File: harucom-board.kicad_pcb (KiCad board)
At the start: 4 copper layers, 91 x 55 mm, 129 parts, among them J1 GT-USB-7010ASV, J2 10.0QCHTZ6.8, J3 HDA65-N1S1-4000-A, J4 PJ-320D, J5 Grove, J6 Grove, J7 PinSocket_1x06, J8 Conn_01x06, Q1 AO3401A, Q2 2N7002, Q3 AO3401A, SW1 PCM12, SW10 TS-1187, SW11 TS-1187, SW2 TS-1088, SW3 TS-1088, SW4 TS-1187, SW5 TS-1187, SW6 TS-1187, SW7 TS-1187, SW8 TS-1187, SW9 TS-1187, U1 H5VU25UC, U10 H5VU25UC, U11 H5VU25UC, U2 AMS1117-3.3, U3 W25Q128JVS, U4 APS6404L-3SQR-SN, U5 RP2350_60QFN, U6 H5VU25UC, U7 NC7WZ16P6X, U8 H5VU25UC, U9 H5VU25UC, Y1 ABM8-272-T3

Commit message: Rev.2 (260322)
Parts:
- removed C33: 100n, Capacitor_SMD:C_0603_1608Metric
- removed the D7 at (136.8, 124.1)
- removed the D8 at (150.2, 126.4)
- removed D9: H5VHD3BC, Diode_SMD:D_SOD-323
- removed the J8 at (167.7, 97.5)
- removed the R27 at (151.5, 99.5)
- removed U10, U11, U8, U9: H5VU25UC, Harucom_Board:Diodes_DFN2510-10L-10_1x2.5mm_P0.5mm
- removed U7: NC7WZ16P6X, Package_TO_SOT_SMD:SOT-363_SC-70-6
- added D3: KT-0603R, LED_SMD:LED_0603_1608Metric, F.Cu at (109.2, 82.8)
- added D5: 1N5819WS, Diode_SMD:D_SOD-323, F.Cu at (152.7, 99.9)
- added G***: LOGO, Harucom_Board:Harukasan_Logo, F.Cu at (140.6, 128.8)
- added J7: Conn_01x04, Connector_PinHeader_2.54mm:PinHeader_1x04_P2.54mm_Vertical, F.Cu at (150.1, 124.5)
- added Q4: AO3401A, Package_TO_SOT_SMD:SOT-23, F.Cu at (170.8, 97.1)
- added R46: 100, Resistor_SMD:R_0603_1608Metric, F.Cu at (110.3, 102.2)
- added R47: 100, Resistor_SMD:R_0603_1608Metric, F.Cu at (110.3, 100.6)
- added R48: 22, Resistor_SMD:R_0603_1608Metric, F.Cu at (180.3, 93.4)
- added R49: 22, Resistor_SMD:R_0603_1608Metric, F.Cu at (178.7, 93.4)
- added R50: 22, Resistor_SMD:R_0603_1608Metric, F.Cu at (176.9, 93.4)
- added R51: 22, Resistor_SMD:R_0603_1608Metric, F.Cu at (175.3, 93.4)
- added R52: 100, Resistor_SMD:R_0603_1608Metric, F.Cu at (139.3, 119.9)
- added R53: 100, Resistor_SMD:R_0603_1608Metric, F.Cu at (139.3, 121.5)
- added R54: 10k, Resistor_SMD:R_0603_1608Metric, F.Cu at (156.6, 125.8)
- added R55: 22, Resistor_SMD:R_0603_1608Metric, F.Cu at (158.2, 125.8)
- added R56: 22, Resistor_SMD:R_0603_1608Metric, F.Cu at (160.5, 125.9)
- added R57: 22, Resistor_SMD:R_0603_1608Metric, F.Cu at (162.1, 125.9)
- added R58: 22, Resistor_SMD:R_0603_1608Metric, F.Cu at (164.2, 125.9)
- added R7: 220, Resistor_SMD:R_0402_1005Metric, F.Cu at (109.2, 84.3)
- C23: footprint Capacitor_SMD:C_0402_1005Metric -> Capacitor_SMD:C_0603_1608Metric
- C24, C25: value 100n -> 220n
- C28, C29: footprint Harucom_Board:C_0402_1005Metric_Pad0.47x0.53mm -> Capacitor_SMD:C_0603_1608Metric
- D6: value H5VHD3BC -> 1N5819WS
- H1, H2, H3, H4: footprint MountingHole:MountingHole_2.2mm_M2_ISO14580 -> MountingHole:MountingHole_2.7mm_M2.5_Pad_Via
- J6: value Grove -> Conn_01x05; footprint Connector:NS-Tech_Grove_1x04_P2mm_Vertical -> Connector_PinSocket_2.54mm:PinSocket_1x05_P2.54mm_Vertical
- NT1: moved to B.Cu
- R14: renamed from R13; footprint Resistor_SMD:R_0402_1005Metric -> Resistor_SMD:R_0603_1608Metric
- R15: renamed from R14; footprint Resistor_SMD:R_0402_1005Metric -> Resistor_SMD:R_0603_1608Metric
- R28, R29, R30, R31, R32, R33, R34, R35, R36, R37, R38, R39, R40, R41, R42, R43: footprint Resistor_SMD:R_0402_1005Metric -> Resistor_SMD:R_0603_1608Metric
- R6: value 100 -> 2.2k; footprint Harucom_Board:R_0402_1005Metric_Pad0.566x0.54mm -> Resistor_SMD:R_0402_1005Metric
- SW1: value PCM12 -> SK-12; footprint Button_Switch_SMD:SW_SPDT_PCM12 -> Harucom_Board:SW_Slide_SPDT_Angled_SK_12D11VG3
- SW10: renamed from SW8; value TS-1187 -> TS6612TP; footprint Button_Switch_SMD:SW_Push_1P1T_XKB_TS-1187A -> Harucom_Board:KEY-SMD_4P-L6.0-W6.0-P4.50-LS9.0
- SW11: renamed from SW9; value TS-1187 -> TS6612TP; footprint Button_Switch_SMD:SW_Push_1P1T_XKB_TS-1187A -> Harucom_Board:KEY-SMD_4P-L6.0-W6.0-P4.50-LS9.0
- SW4, SW5, SW6, SW7: value TS-1187 -> TS6612TP; footprint Button_Switch_SMD:SW_Push_1P1T_XKB_TS-1187A -> Harucom_Board:KEY-SMD_4P-L6.0-W6.0-P4.50-LS9.0
- SW8: renamed from SW10; value TS-1187 -> TS6612TP; footprint Button_Switch_SMD:SW_Push_1P1T_XKB_TS-1187A -> Harucom_Board:KEY-SMD_4P-L6.0-W6.0-P4.50-LS9.0
- SW9: renamed from SW11; value TS-1187 -> TS6612TP; footprint Button_Switch_SMD:SW_Push_1P1T_XKB_TS-1187A -> Harucom_Board:KEY-SMD_4P-L6.0-W6.0-P4.50-LS9.0
- moved J6 67.1 mm to (188.2, 87.7), turned to -90 degrees
- moved D6 41.6 mm to (151.2, 94.7), turned to 0 degrees
- moved C23 20.6 mm to (151.0, 93.0), turned to 0 degrees
- moved SW2 16.7 mm to (188.8, 99.1), turned to 90 degrees
- moved SW3 14.7 mm to (188.8, 92.7), turned to -90 degrees
- moved J5 10.6 mm to (104.7, 106.5), turned to 180 degrees
- moved R14 10.3 mm to (183.3, 96.1), turned to 90 degrees
- moved R15 9.17 mm to (183.3, 91.5), turned to 90 degrees
- moved C31 7.97 mm to (144.3, 118.9), turned to -90 degrees
- moved C32 4.36 mm to (154.3, 126.7)
- moved J8 4.04 mm to (152.7, 129.6)
- moved R16 3.98 mm to (169.7, 102.4)
- moved Q3 3.94 mm to (169.7, 99.9)
- moved G*** 3.91 mm to (178.6, 102.8)
- moved R45 3.90 mm to (133.1, 107.4)
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- renumbered C12 to C11, C11 to C12, C6 to C4, C8 to C5, C4 to C6, C5 to C7, C7 to C8, D3 to D4, D4 to D7, D5 to D8, J7 to J8, R8 to R10, R10 to R11, R11 to R12, R12 to R13, R15 to R16, R16 to R17, R17 to R18, R18 to R19, R19 to R20, R20 to R21, R21 to R22, R22 to R23, R23 to R24, R24 to R25, R25 to R26, R26 to R27, R7 to R8
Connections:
- C23 pad 1: +3V3 -> Net-(D6-K)
- D6 pad 1: +5V -> Net-(D6-K)
- D6 pad 2: GND -> +5V
- J3 pad 18: +5V -> Net-(D6-K)
- J5 pad 1: GND -> Net-(J5-Pin_1)
- J5 pad 2: +5V -> Net-(J5-Pin_2)
- J5 pad 3: /I2C0_SDA -> +5V
- J5 pad 4: /I2C0_SDL -> GND
- J6 pad 2: +3V3 -> Net-(J6-Pin_2)
- J6 pad 3: /UART1_TX -> Net-(J6-Pin_3)
- J6 pad 4: /UART1_RX -> Net-(J6-Pin_4)
- J8 pad 3: /SPI0_CS -> Net-(J8-Pin_3)
- J8 pad 4: /SPI0_RX -> Net-(J8-Pin_4)
- J8 pad 5: /SPI0_TX -> Net-(J8-Pin_5)
- J8 pad 6: /SPI0_SCK -> Net-(J8-Pin_6)
- Q3 pad 3: /USB Host/VBUS -> Net-(Q3-D)
- R27 pad 1: /DVI_HPD -> Net-(J3-HPD)
- R27 pad 2: Net-(J3-HPD) -> /DVI_HPD
- R28 pad 1: Net-(R28-Pad1) -> /RP2350A/GPIO24
- R29 pad 1: Net-(R29-Pad1) -> /RP2350A/GPIO25
- R3 pad 1: Net-(D1-A1) -> Net-(Q1-G)
- R3 pad 2: Net-(Q1-G) -> GND
- R45 pad 2: /I2C0_SDL -> /I2C0_SCL
- SW1 pad : (no net) -> GND
- SW1 pad 1: GND -> Net-(D1-A1)
- U5 pad 3: /RP2350A/GPIO1 -> /ERR_LED
- U5 pad 33: /I2C0_SDL -> /I2C0_SCL
- U5 pad 40: /UART1_RX -> /I2C1_SDA
- U5 pad 41: /UART1_TX -> /I2C1_SCL
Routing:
- net /ERR_LED: track 0.00 -> 67.6 mm, vias 0 -> 4
- net /I2C0_SDL: track 43.7 -> 0.00 mm, vias 3 -> 0
- net /I2C0_SCL: track 0.00 -> 38.3 mm, vias 0 -> 3
- net /UART1_RX: track 34.1 -> 0.00 mm, vias 2 -> 0
- net /UART1_TX: track 32.3 -> 0.00 mm, vias 2 -> 0
- net /I2C1_SDA: track 0.00 -> 24.3 mm, vias 0 -> 2
- net /I2C1_SCL: track 0.00 -> 22.7 mm, vias 0 -> 2
- net +5V: track 128.0 -> 113.0 mm, vias 5 -> 4
- net +3V3: track 91.0 -> 76.4 mm
- net GND: track 59.9 -> 70.2 mm, vias 283 -> 331
- net Net-(J5-Pin_1): track 0.00 -> 8.84 mm
- net Net-(J6-Pin_2): track 0.00 -> 8.26 mm
- net Net-(J6-Pin_3): track 0.00 -> 8.17 mm
- net Net-(J7-Pin_3): track 0.00 -> 8.16 mm
- net /SWCLK: track 56.0 -> 48.2 mm
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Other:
- outline, holes or cut-outs redrawn
- board text added: "GND 5V SDA SCL"
- board text added: "Harucom-board Rev.2 (260322) ©2026 Shunsuke Michii Licesensed under CERN-OHL-P-2.0"
- board text added: "SDA SCL 3V3"
- board text added: "TX RX SWDIO SWCLK GND"
- board text removed: "5V"
- board text removed: "HARUCOM 260304 ©2026 harukasan"
- board text removed: "POWER"
- board text removed: "R"
- board text removed: "RubyKaigi 2026 Logo: This work by RubyKaigi 2026 Team is licensed under CC BY 4.0. https://rubykaigi.org/2026/goodies/"
- board text removed: "SDA"
- board text removed: "SDL"
- board text removed: "SWCLK"
- board text removed: "SWDIO"
- board text removed: "T"

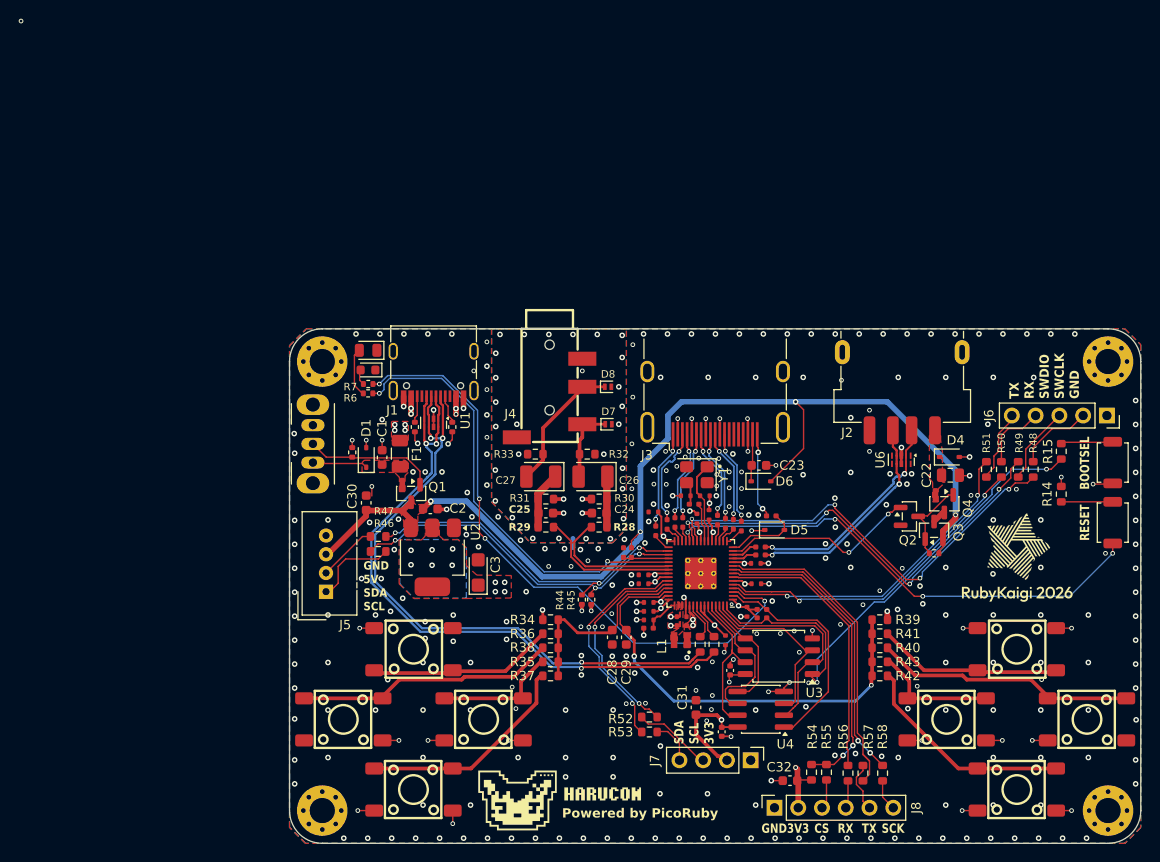
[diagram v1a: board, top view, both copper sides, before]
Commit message: Rev. 2B: Change PSRAM package from SOP-8 to USON-8L.
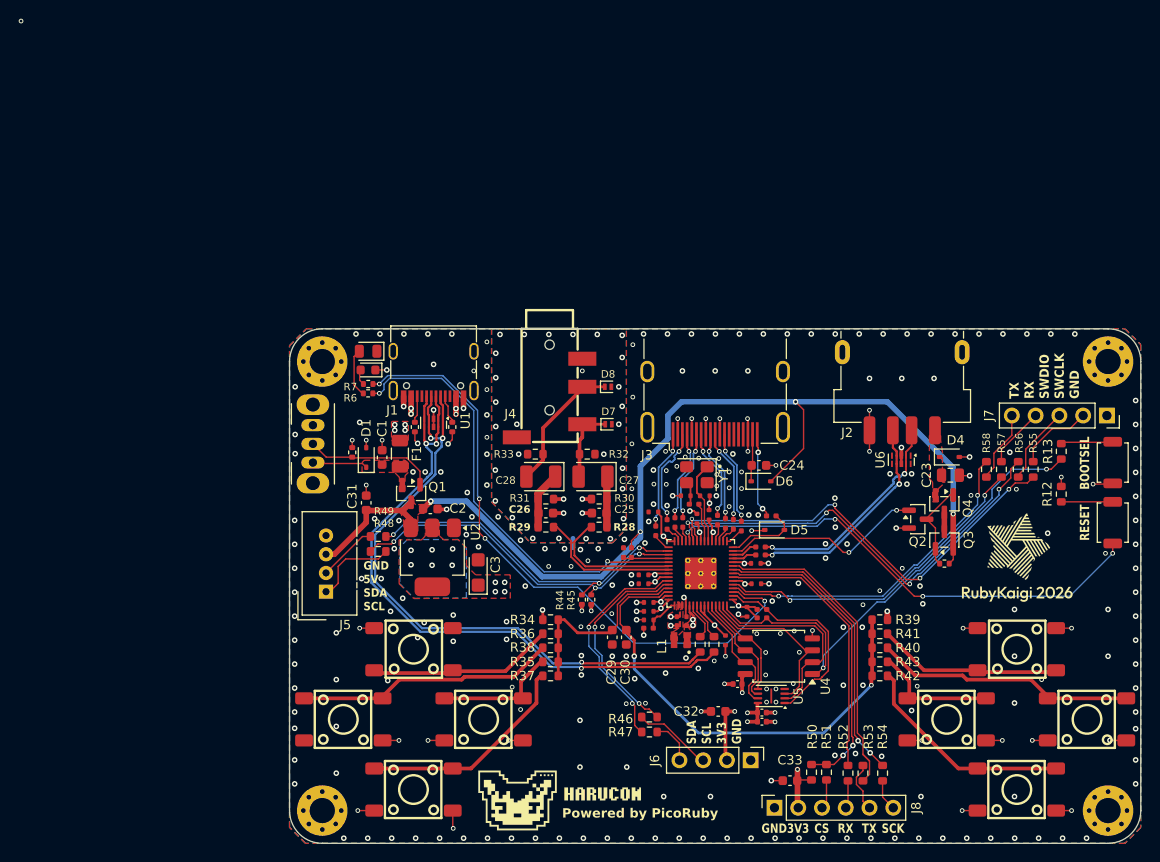
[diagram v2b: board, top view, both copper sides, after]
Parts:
- removed the C11 at (147.0, 121.5)
- removed the U4 at (151.2, 119.1)
- added C21: 1u, Capacitor_SMD:C_0402_1005Metric, F.Cu at (151.3, 120.4)
- added C22: 100n, Capacitor_SMD:C_0402_1005Metric, F.Cu at (151.3, 119.4)
- added U5: APS6404L-3SQRx-ZR, Package_SON:Winbond_USON-8-1EP_3x2mm_P0.5mm_EP0.2x1.6mm, F.Cu at (152.3, 117.7)
- moved C32 2.41 mm to (146.7, 119.3), turned to 0 degrees
- moved C20 1.66 mm to (148.7, 116.4), turned to 180 degrees
- moved R16 1.56 mm to (170.8, 103.5)
- moved Q3 1.52 mm to (170.8, 101.0)
- moved Q2 0.95 mm to (168.0, 98.8)
- moved D2 0.10 mm to (109.2, 80.8)
- renumbered C14 to C10, C15 to C11, C16 to C12, C17 to C13, C18 to C14, C19 to C15, C20 to C16, C21 to C17, C6 to C18, C7 to C19, C8 to C20, C22 to C23, C23 to C24, C24 to C25, C25 to C26, C26 to C27, C27 to C28, C28 to C29, C29 to C30, C30 to C31, C31 to C32, C32 to C33, C9 to C6, C10 to C7, C12 to C8, C13 to C9, J7 to J6, J6 to J7, R13 to R10, R10 to R11, R14 to R12, R15 to R13, R8 to R14, R11 to R15, R52 to R46, R53 to R47, R46 to R48, R47 to R49, R54 to R50, R55 to R51, R56 to R52, R57 to R53, R58 to R54, R48 to R55, R49 to R56, R50 to R57, R51 to R58, R9 to R8, R12 to R9, U5 to U3, U3 to U4
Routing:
- net GND: track 70.2 -> 79.4 mm, vias 331 -> 300
- net /RP2350A/QSPI_SS: track 57.0 -> 53.3 mm
- net /RP2350A/QSPI_SD3: track 16.2 -> 12.6 mm
- net +3V3: track 76.4 -> 72.9 mm, vias 28 -> 30
- net /RP2350A/GPIO29_ADC3: track 46.8 -> 50.1 mm
- net /RP2350A/QSPI_SCLK: track 14.6 -> 11.5 mm
- net /RP2350A/PSRAM_CS: track 24.4 -> 22.0 mm
- net /RP2350A/QSPI_SD0: track 12.2 -> 10.5 mm
- net /RP2350A/QSPI_SD1: track 22.8 -> 21.5 mm
- net /USBH_EN: track 20.7 -> 21.9 mm
- net /RP2350A/QSPI_SD2: track 19.5 -> 18.4 mm
- net +5V: track 113.0 -> 113.9 mm
- net Net-(J7-Pin_4): track 7.11 -> 6.22 mm
- net Net-(Q3-D): track 1.50 -> 2.01 mm
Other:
- board text added: "Harucom-board Rev.2B (260323) ©2026 Shunsuke Michii Licesensed under CERN-OHL-P-2.0"
- board text added: "SDA SCL 3V3 GND"
- board text removed: "Harucom-board Rev.2 (260322) ©2026 Shunsuke Michii Licesensed under CERN-OHL-P-2.0"
- board text removed: "SDA SCL 3V3"

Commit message: Refine wireing
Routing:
- net /USB_D-: track 68.0 -> 70.0 mm
- net +3V3: track 72.9 -> 74.2 mm

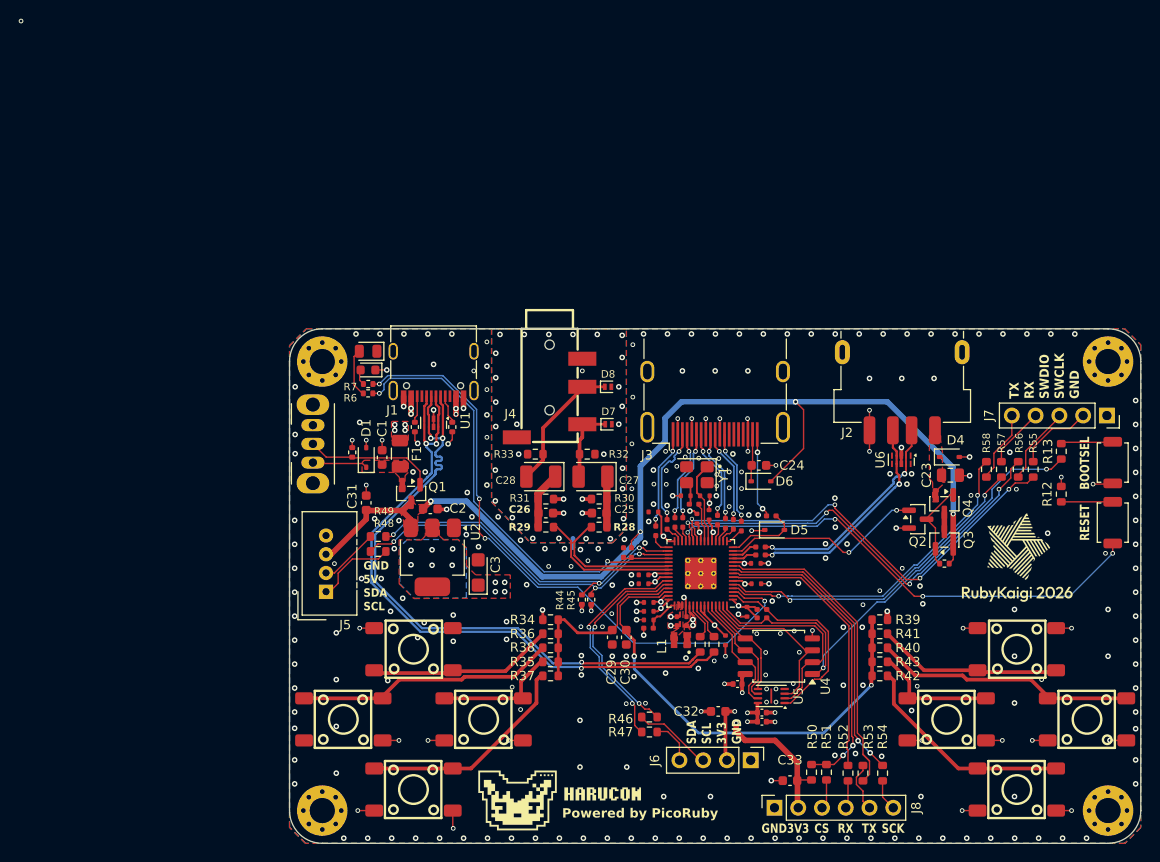
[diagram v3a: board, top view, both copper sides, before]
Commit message: Rev. 3B: Disconnect mounting holes from GND
  - Change mounting holes from MountingHole_Pad (with via) to MountingHole (ISO14580)
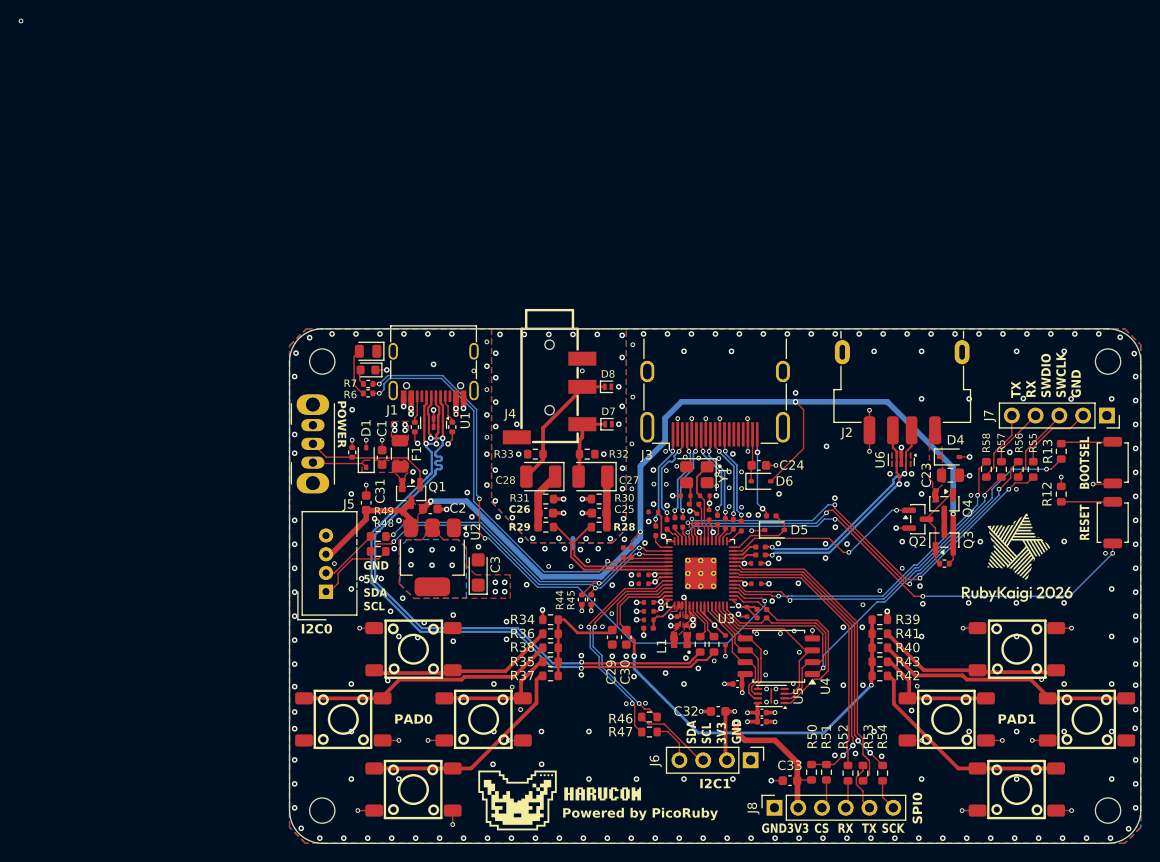
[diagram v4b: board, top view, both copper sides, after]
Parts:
- H1, H2, H3, H4: footprint MountingHole:MountingHole_2.7mm_M2.5_Pad_Via -> MountingHole:MountingHole_2.7mm_M2.5_ISO14580
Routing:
- net GND: track 79.4 -> 77.2 mm, vias 300 -> 344
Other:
- board text added: "Harucom-board Rev.3B (260403) ©2026 Shunsuke Michii Licesensed under CERN-OHL-P-2.0"
- board text added: "I2C0"
- board text added: "I2C1"
- board text added: "PAD0"
- board text added: "PAD1"
- board text added: "POWER"
- board text added: "SPI0"
- board text removed: "Harucom-board Rev.2B (260323) ©2026 Shunsuke Michii Licesensed under CERN-OHL-P-2.0"
